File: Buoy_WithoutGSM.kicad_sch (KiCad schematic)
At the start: 7 parts

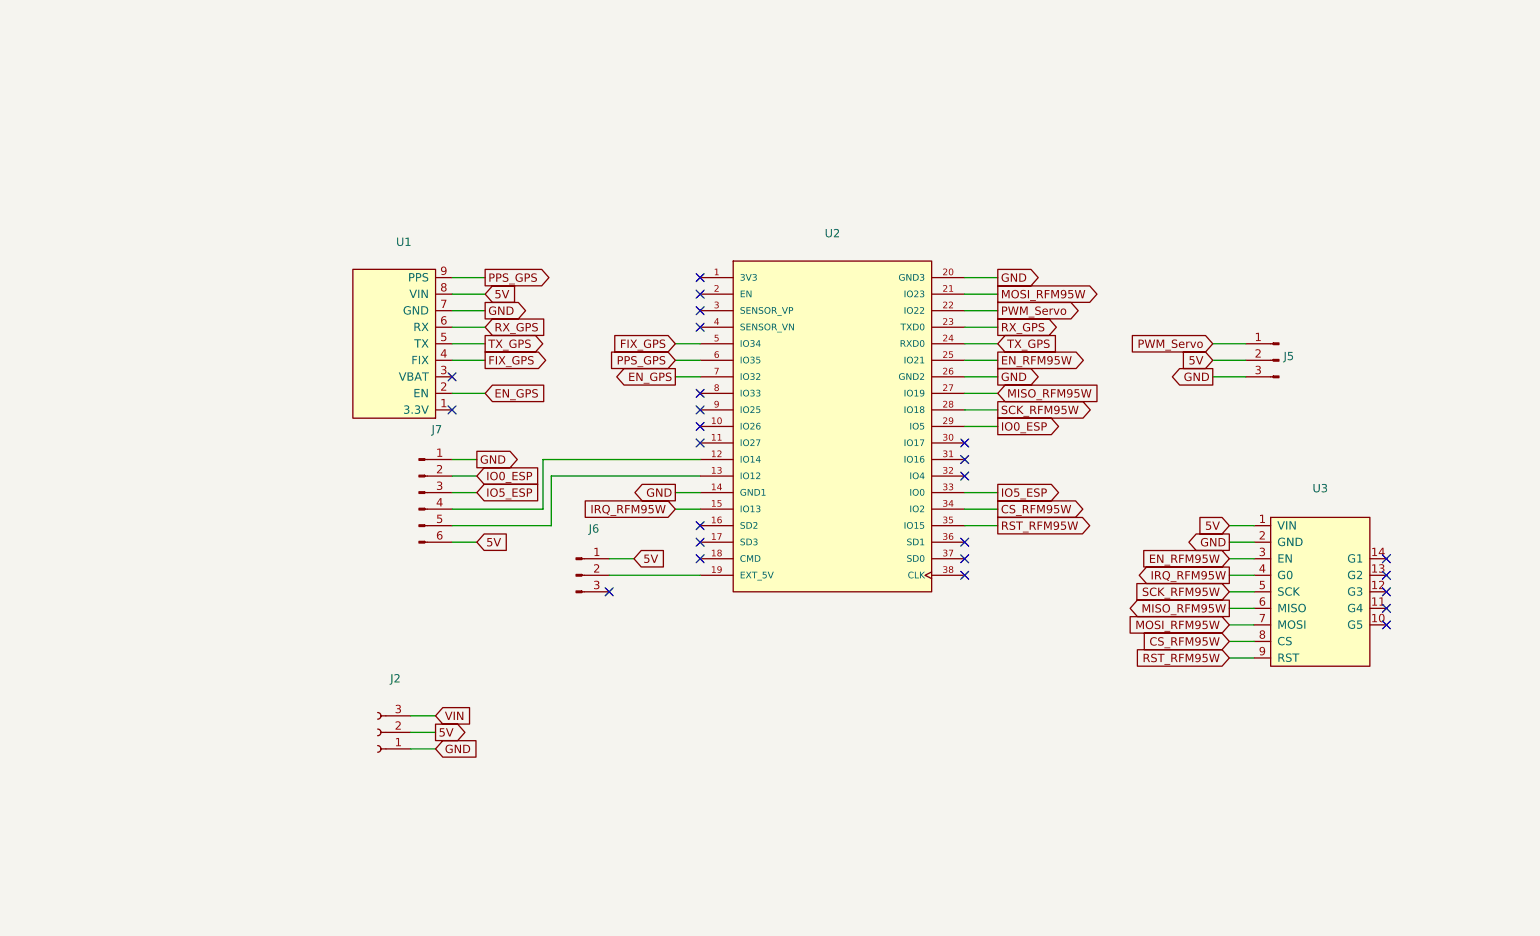
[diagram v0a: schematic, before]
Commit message: Added Ethernet module and input measurement
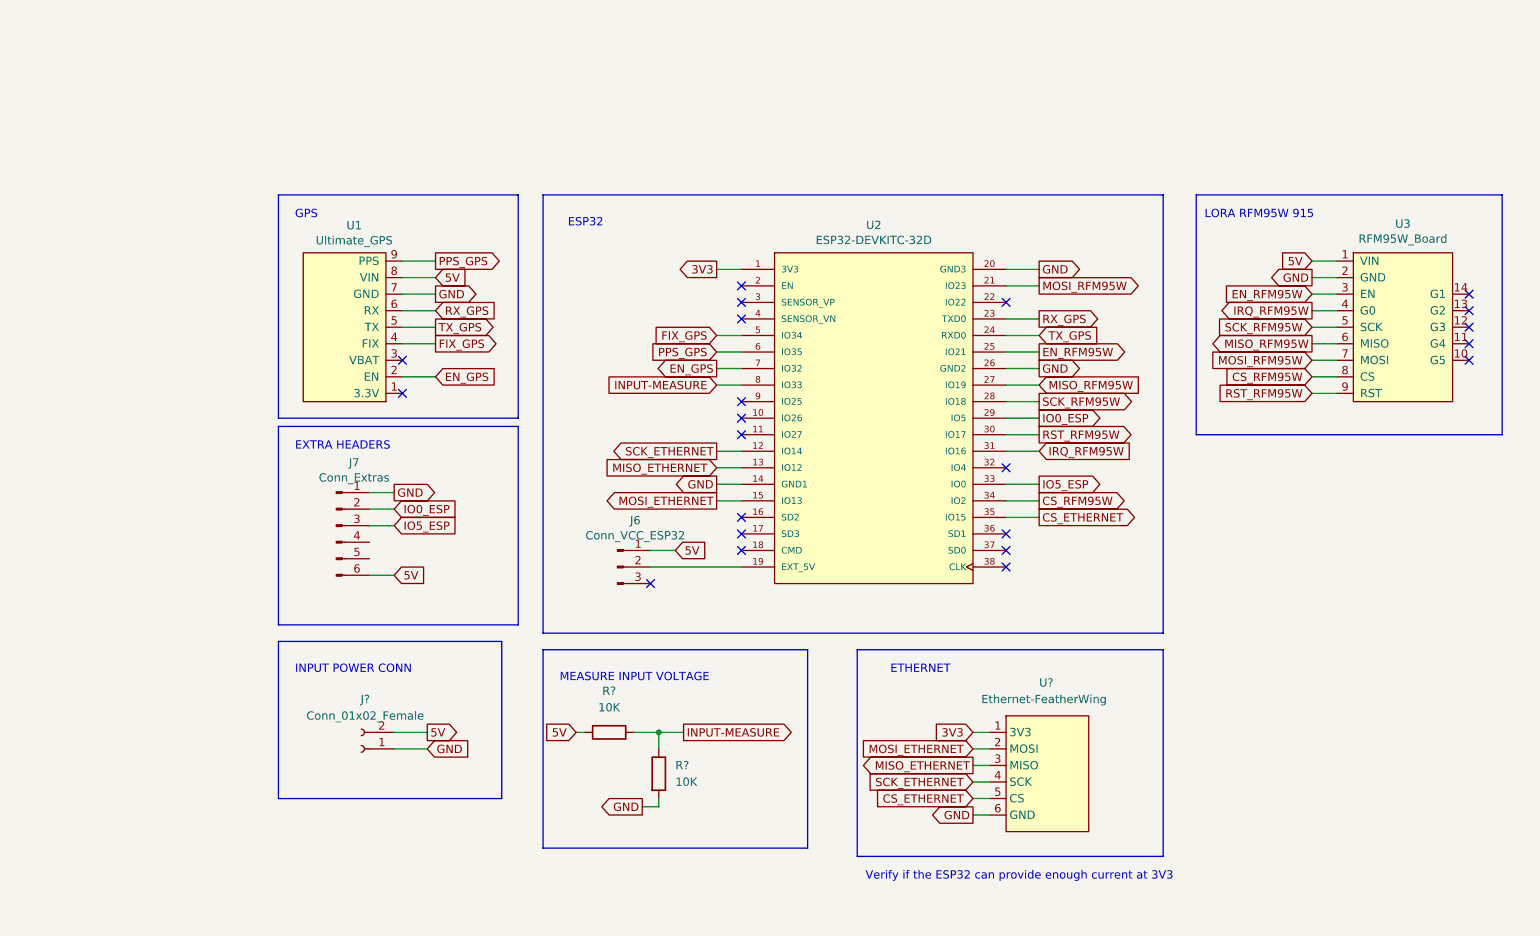
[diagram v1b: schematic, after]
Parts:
- removed J2: (no value), symbol Connector:Conn_01x03_Female
- removed J5: (no value), symbol Connector:Conn_01x03_Male
- added J?: Conn_01x02_Female, symbol Connector:Conn_01x02_Female
- added R? (x2): 10K, Resistor_SMD:R_0805_2012Metric, symbol R-10K-0805:10K
- added U?: Ethernet-FeatherWing, Ethernet-FeatherWing:Ethernet FeatherWing, symbol Ethernet-FeatherWing:Ethernet-FeatherWing
- J6: value (none) -> Conn_VCC_ESP32; footprint (none) -> Connector_PinHeader_2.54mm:PinHeader_1x03_P2.54mm_Vertical
- J7: value (none) -> Conn_Extras; footprint (none) -> Connector_PinHeader_2.54mm:PinHeader_1x06_P2.54mm_Vertical
- U1: value (none) -> Ultimate_GPS; footprint (none) -> Footprints:Ultimate_GPS
- U2: value (none) -> ESP32-DEVKITC-32D; footprint (none) -> Footprints:MODULE_ESP32-DEVKITC-32D
- U3: value (none) -> RFM95W_Board; footprint (none) -> Footprints:RFM95W-Board
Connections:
- net 5V: now also J?.2 (Pin_2), R?.1
- net GND: now also J?.1 (Pin_1), R?.2, U?.6 (GND)
- net IRQ_RFM95W: now also U2.31 (IO16); no longer U2.15 (IO13)
- net RST_RFM95W: now also U2.30 (IO17); no longer U2.35 (IO15)
- net 3V3: now reaches U2.1 (3V3)
- net 3V3: now also U?.1 (3V3)
- net at J7.4 (Pin_4): no longer U2.12 (IO14)
- net at J7.5 (Pin_5): no longer U2.13 (IO12)
- net INPUT-MEASURE: now reaches U2.8 (IO33)
- net INPUT-MEASURE: now also R?.1, R?.2
- net PWM_Servo: no longer names the net of U2.22 (IO22)
- new net CS_ETHERNET: U2.35 (IO15), U?.5 (CS)
- new net MISO_ETHERNET: U2.13 (IO12), U?.3 (MISO)
- new net MOSI_ETHERNET: U2.15 (IO13), U?.2 (MOSI)
- new net SCK_ETHERNET: U2.12 (IO14), U?.4 (SCK)
- no-connect marks 25 -> 22
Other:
- note added: "ESP32"
- note added: "ETHERNET"
- note added: "EXTRA HEADERS"
- note added: "GPS"
- note added: "INPUT POWER CONN"
- note added: "LORA RFM95W 915"
- note added: "MEASURE INPUT VOLTAGE"
- note added: "Verify if the ESP32 can provide enough current at 3V3"
- moved on the sheet: J6, J7, U1, U2, U3

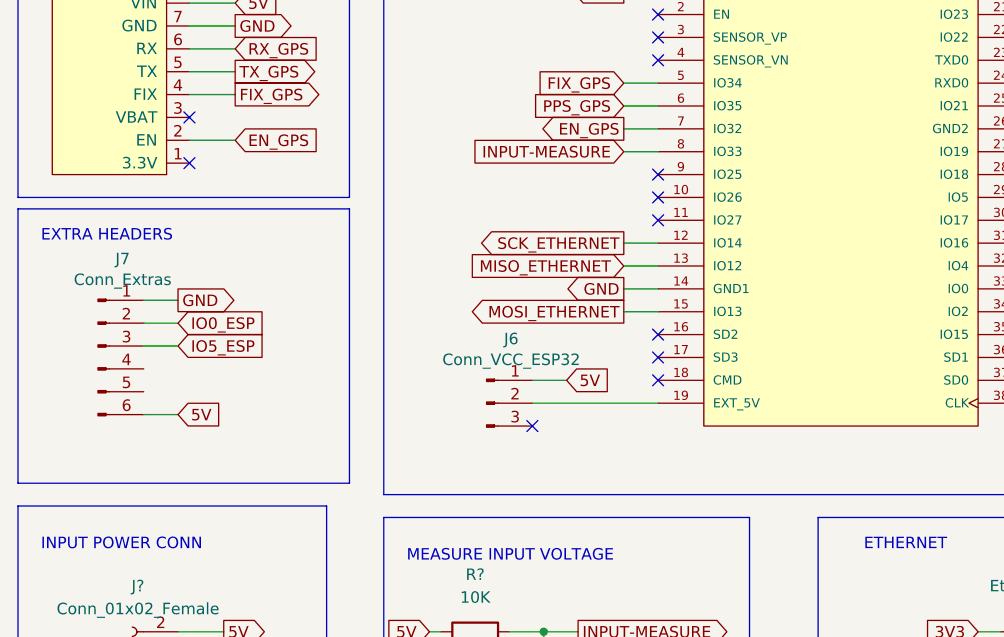
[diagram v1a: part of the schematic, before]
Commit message: Added connections to the Extra Conn
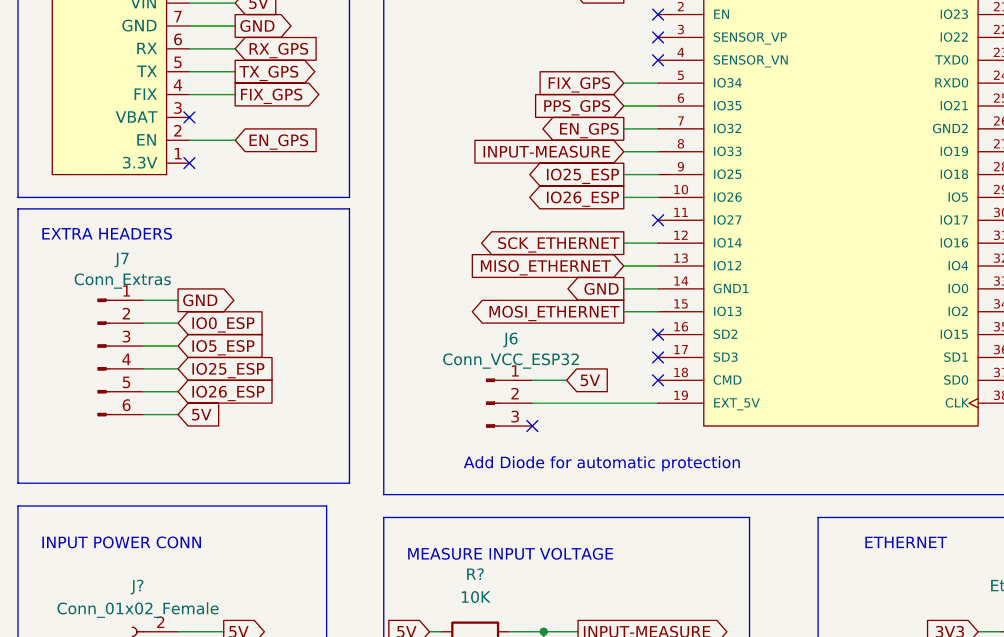
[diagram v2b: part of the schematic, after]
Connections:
- net IO26_ESP: now reaches U2.10 (IO26)
- net IO26_ESP: now also J7.5 (Pin_5)
- net IO25_ESP: now reaches U2.9 (IO25)
- net IO25_ESP: now also J7.4 (Pin_4)
- no-connect marks 22 -> 20
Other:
- note added: "Add Diode for automatic protection"
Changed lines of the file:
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@@
   (no_connect (at 255.27 76.2))
   (no_connect (at 184.15 92.71))
-  (no_connect (at 143.51 85.09))
-  (no_connect (at 143.51 82.55))
   (no_connect (at 143.51 87.63))
   (wire (pts (xy 184.15 95.25) (xy 189.23 95.25))
@@
     (stroke (width 0) (type default) (color 0 0 0 0))
   )
+  (wire (pts (xy 139.7 85.09) (xy 143.51 85.09))
+    (stroke (width 0) (type default) (color 0 0 0 0))
+  )
   (wire (pts (xy 96.52 60.96) (xy 91.44 60.96))
     (stroke (width 0) (type default) (color 0 0 0 0))
@@
     (stroke (width 0) (type default) (color 0 0 0 0))
   )
+  (wire (pts (xy 86.36 106.68) (xy 90.17 106.68))
+    (stroke (width 0) (type default) (color 0 0 0 0))
+  )
   (polyline (pts (xy 72.39 119.38) (xy 72.39 143.51))
     (stroke (width 0) (type default) (color 0 0 0 0))
   )
+  (wire (pts (xy 86.36 104.14) (xy 90.17 104.14))
+    (stroke (width 0) (type default) (color 0 0 0 0))
+  )
   (polyline (pts (xy 72.39 116.84) (xy 109.22 116.84))
     (stroke (width 0) (type default) (color 0 0 0 0))
   )
+  (wire (pts (xy 139.7 82.55) (xy 143.51 82.55))
+    (stroke (width 0) (type default) (color 0 0 0 0))
+  )
   (wire (pts (xy 130.81 133.35) (xy 127 133.35))
     (stroke (width 0) (type default) (color 0 0 0 0))
@@
   )
   (text "ESP32" (at 116.84 55.88 0)
+    (effects (font (size 1.27 1.27)) (justify left bottom))
+  )
+  (text "Add Diode for automatic protection" (at 121.92 115.57 0)
     (effects (font (size 1.27 1.27)) (justify left bottom))
   )
@@
     )
   )
+  (global_label "IO26_ESP" (shape output) (at 139.7 85.09 180) (fields_autoplaced)
+    (effects (font (size 1.27 1.27)) (justify right))
+    (property "Intersheet References" "${INTERSHEET_REFS}" (id 0) (at 128.4253 85.0106 0)
+      (effects (font (size 1.27 1.27)) (justify right) hide)
+    )
+  )
   (global_label "IRQ_RFM95W" (shape output) (at 231.14 68.58 180) (fields_autoplaced)
     (effects (font (size 1.27 1.27)) (justify right))
@@
     )
   )
+  (global_label "IO26_ESP" (shape input) (at 90.17 106.68 0) (fields_autoplaced)
+    (effects (font (size 1.27 1.27)) (justify left))
+    (property "Intersheet References" "${INTERSHEET_REFS}" (id 0) (at 101.4447 106.6006 0)
+      (effects (font (size 1.27 1.27)) (justify left) hide)
+    )
+  )
   (global_label "GND" (shape output) (at 231.14 63.5 180) (fields_autoplaced)
     (effects (font (size 1.27 1.27)) (justify right))
@@
     )
   )
+  (global_label "IO25_ESP" (shape input) (at 90.17 104.14 0) (fields_autoplaced)
+    (effects (font (size 1.27 1.27)) (justify left))
+    (property "Intersheet References" "${INTERSHEET_REFS}" (id 0) (at 101.4447 104.0606 0)
+      (effects (font (size 1.27 1.27)) (justify left) hide)
+    )
+  )
   (global_label "SCK_ETHERNET" (shape output) (at 139.7 90.17 180) (fields_autoplaced)
     (effects (font (size 1.27 1.27)) (justify right))
@@
     )
   )
+  (global_label "IO25_ESP" (shape output) (at 139.7 82.55 180) (fields_autoplaced)
+    (effects (font (size 1.27 1.27)) (justify right))
+    (property "Intersheet References" "${INTERSHEET_REFS}" (id 0) (at 128.4253 82.4706 0)
+      (effects (font (size 1.27 1.27)) (justify right) hide)
+    )
+  )

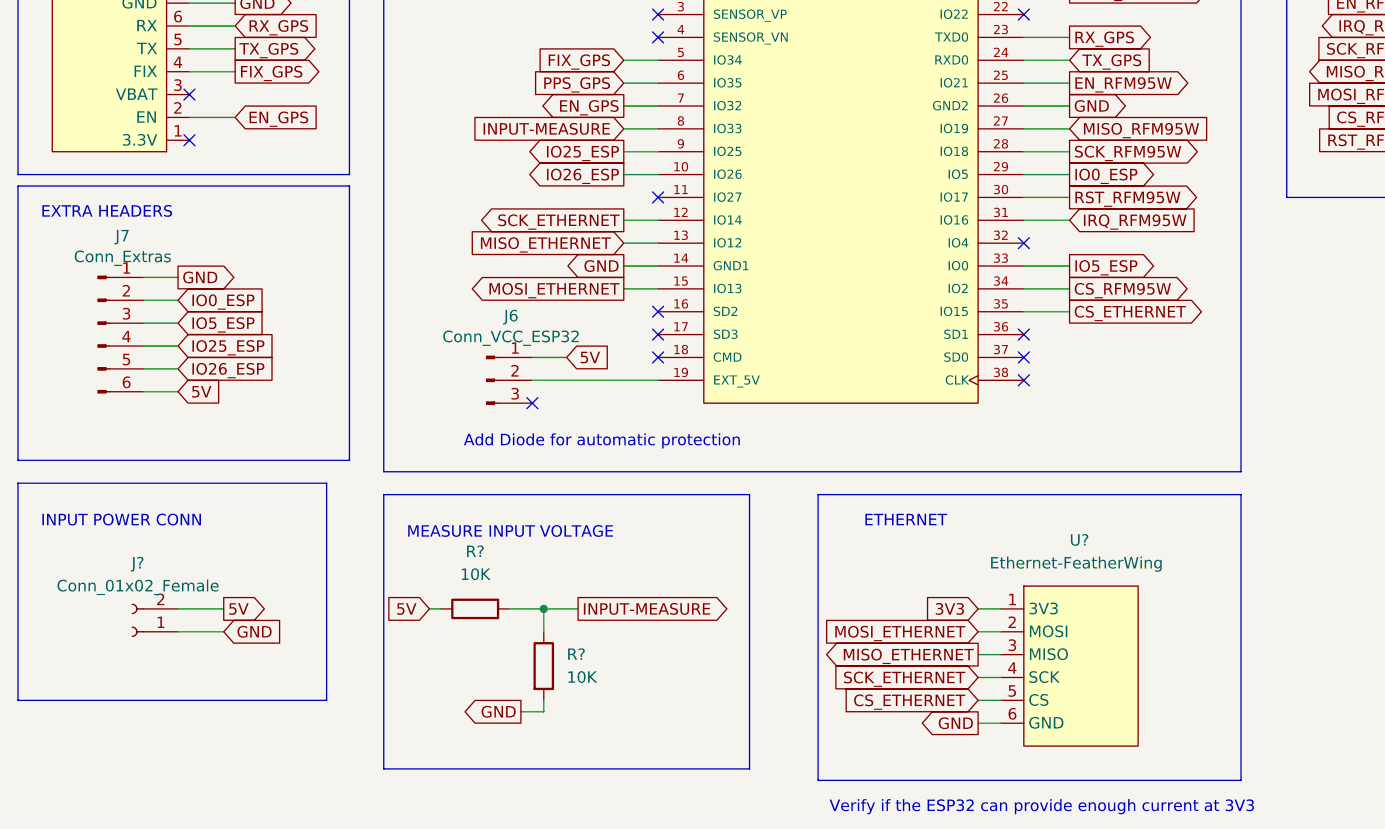
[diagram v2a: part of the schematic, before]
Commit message: Added 3D model for the Ethernet module and routed changes on PCB
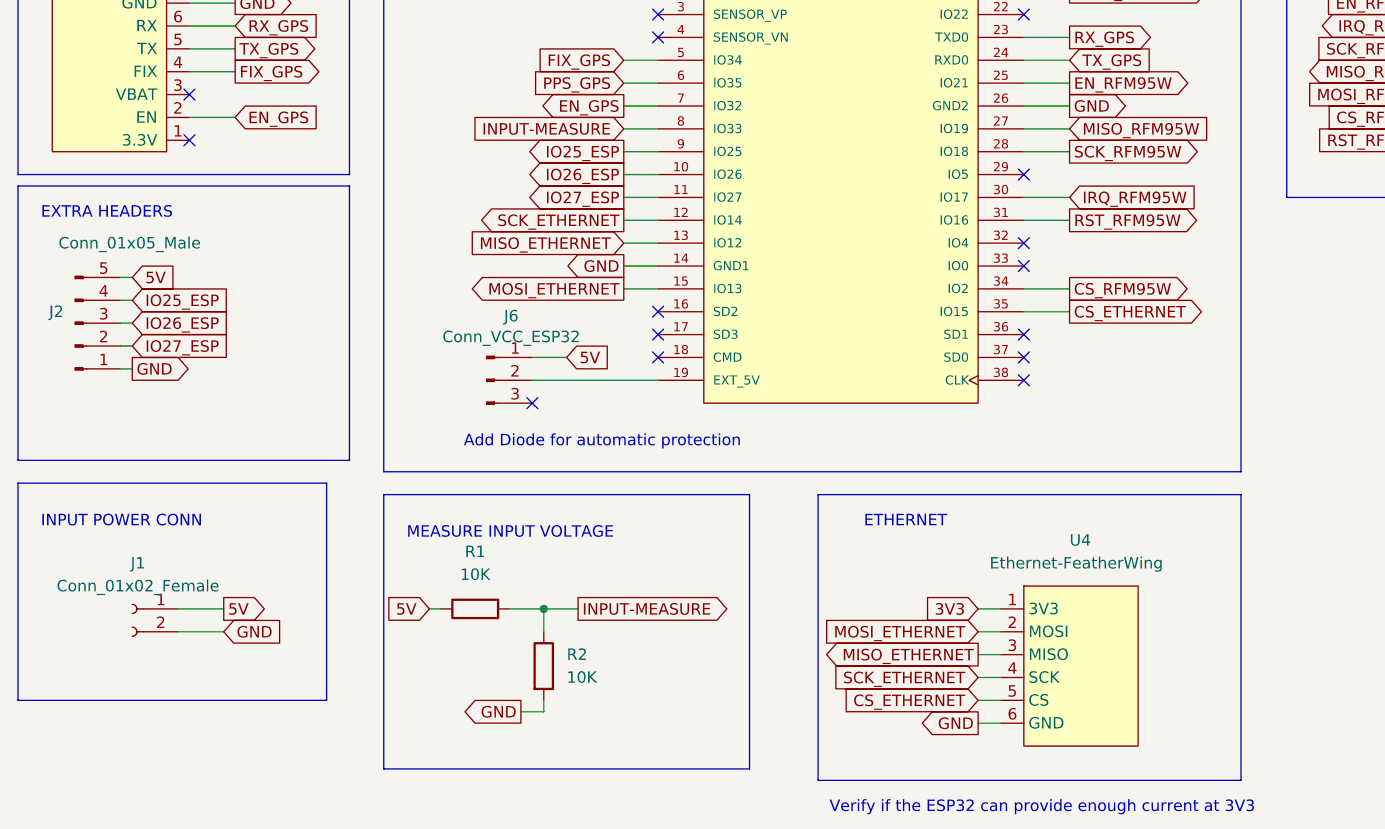
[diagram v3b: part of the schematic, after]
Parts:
- removed J7: Conn_Extras, Connector_PinHeader_2.54mm:PinHeader_1x06_P2.54mm_Vertical, symbol Connector:Conn_01x06_Male
- added J2: Conn_01x05_Male, Connector_PinSocket_2.54mm:PinSocket_1x05_P2.54mm_Vertical, symbol Connector:Conn_01x05_Male
- J1: renamed from J?; footprint (none) -> TerminalBlock:TerminalBlock_bornier-2_P5.08mm
- gave numbers to parts that had none: 3
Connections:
- net 5V: now also J1.1 (Pin_1), J2.5 (Pin_5); no longer J1.2 (Pin_2)
- net GND: now also J1.2 (Pin_2), J2.1 (Pin_1); no longer J1.1 (Pin_1)
- net IO25_ESP: now also J2.4 (Pin_4)
- net IO26_ESP: now also J2.3 (Pin_3)
- net IRQ_RFM95W: now also U2.30 (IO17); no longer U2.31 (IO16)
- net RST_RFM95W: now also U2.31 (IO16); no longer U2.30 (IO17)
- net IO27_ESP: now reaches U2.11 (IO27)
- net IO27_ESP: now also J2.2 (Pin_2)
- net IO0_ESP: no longer names the net of U2.29 (IO5)
- net IO5_ESP: no longer names the net of U2.33 (IO0)
- no-connect marks 20 -> 21
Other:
- moved on the sheet: J1
